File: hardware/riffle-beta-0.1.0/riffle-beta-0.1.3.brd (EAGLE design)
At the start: 104.8 x 18 mm, 46 parts, among them IC1 ATMEGA328P, IC3 CH340G, IC4 MCP1700-33, IC5 24AA128SN, IC6 MCP1700-33, J1 AYZ0202, U1 MCP73831T-2ACI/OT, X2 12MHz, X3 16 MHz

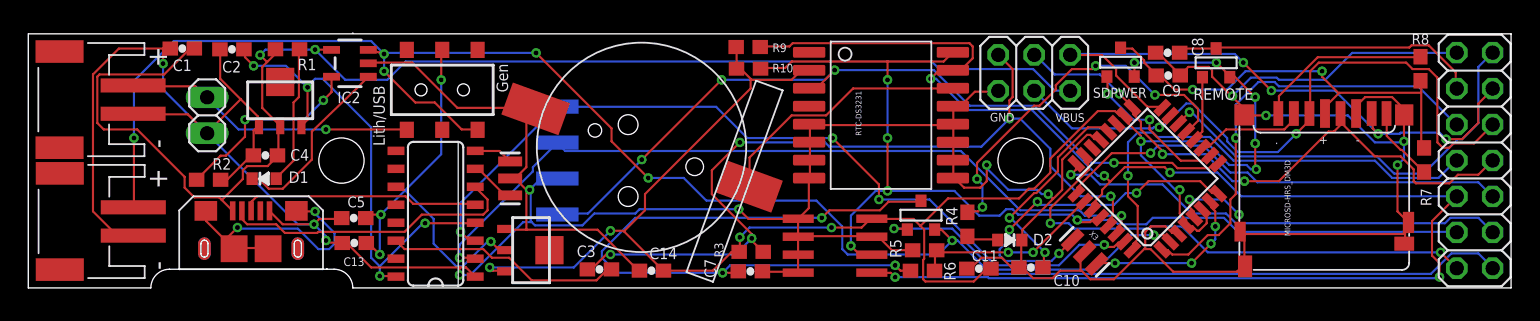
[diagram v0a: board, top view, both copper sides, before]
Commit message: tightened USB cutout; moved via away from left screw
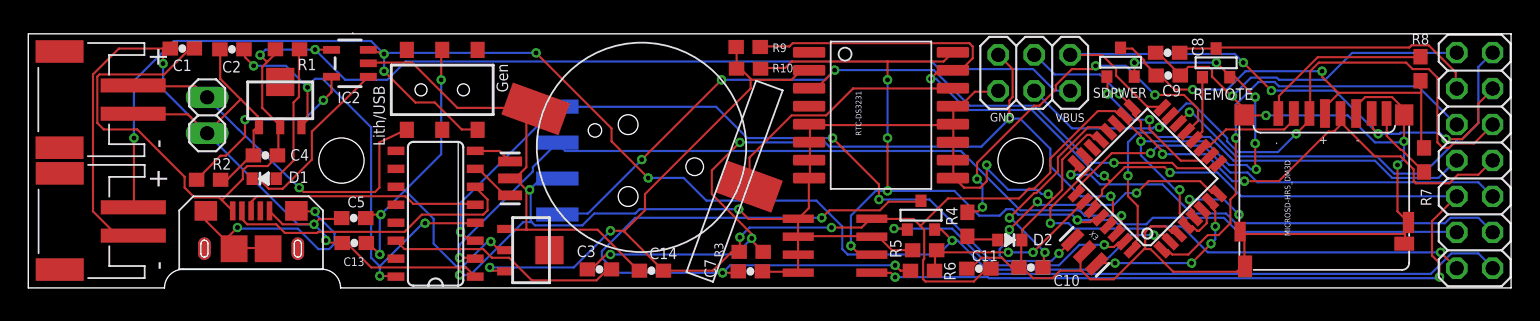
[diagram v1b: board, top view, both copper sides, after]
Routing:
- net VGEN: track 20.7 -> 26.0 mm
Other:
- outline, holes or cut-outs redrawn
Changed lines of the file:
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@@
 <text x="1.5494" y="2.54" size="1.016" layer="22" rot="MR90">3.7V</text>
 <wire x1="-2.1336" y1="17.9578" x2="102.6668" y2="17.9578" width="0" layer="20"/>
-<wire x1="20.8026" y1="0" x2="102.6668" y2="0" width="0" layer="20"/>
+<wire x1="19.939" y1="0" x2="102.6668" y2="0" width="0" layer="20"/>
 <wire x1="102.6668" y1="17.9578" x2="102.6668" y2="0" width="0" layer="20"/>
-<wire x1="-2.1336" y1="0" x2="6.5278" y2="0" width="0" layer="20"/>
-<wire x1="6.5278" y1="0" x2="7.8486" y2="1.3208" width="0" layer="20" curve="-90"/>
-<wire x1="7.8486" y1="1.3208" x2="18.9738" y2="1.3208" width="0" layer="20"/>
-<wire x1="18.9738" y1="1.3208" x2="18.9738" y2="1.3462" width="0" layer="20"/>
-<wire x1="18.9738" y1="1.3208" x2="19.4818" y2="1.3208" width="0" layer="20"/>
-<wire x1="19.4818" y1="1.3208" x2="20.8026" y2="0" width="0" layer="20" curve="-90"/>
+<wire x1="-2.1336" y1="0" x2="7.493" y2="0" width="0" layer="20"/>
+<wire x1="7.493" y1="0" x2="8.8138" y2="1.3208" width="0" layer="20" curve="-90"/>
+<wire x1="8.8138" y1="1.3208" x2="18.6182" y2="1.3208" width="0" layer="20"/>
+<wire x1="18.6182" y1="1.3208" x2="19.939" y2="0" width="0" layer="20" curve="-90"/>
 <text x="65.8368" y="11.7602" size="0.6096" layer="21">GND</text>
 <text x="70.4596" y="11.7348" size="0.6096" layer="21">VBUS</text>
@@
 <contactref element="J1" pad="4"/>
 <contactref element="JP1" pad="2"/>
-<wire x1="18.8976" y1="11.2014" x2="24.6126" y2="11.2014" width="0.1524" layer="1"/>
-<wire x1="12.7254" y1="11.2014" x2="18.8976" y2="11.2014" width="0.1524" layer="16"/>
+<wire x1="17.018" y1="7.0866" x2="17.3228" y2="6.7818" width="0.1524" layer="1"/>
+<wire x1="17.3228" y1="6.7818" x2="22.3774" y2="6.7818" width="0.1524" layer="1"/>
+<wire x1="22.3774" y1="6.7818" x2="22.6822" y2="7.0866" width="0.1524" layer="1"/>
+<wire x1="22.6822" y1="7.0866" x2="22.6822" y2="10.287" width="0.1524" layer="1"/>
+<wire x1="22.6822" y1="10.287" x2="24.6126" y2="11.2014" width="0.1524" layer="1"/>
+<wire x1="12.7254" y1="11.2014" x2="17.018" y2="7.0866" width="0.1524" layer="16"/>
 <wire x1="10.5156" y1="13.4112" x2="12.7254" y2="11.2014" width="0.1524" layer="16"/>
 <wire x1="24.6126" y1="11.2014" x2="24.6226" y2="11.1742" width="0.1524" layer="1"/>
@@
 <wire x1="5.334" y1="14.2494" x2="5.2748" y2="14.3096" width="0.1524" layer="1"/>
 <wire x1="10.4394" y1="13.4874" x2="10.509" y2="13.4696" width="0.1524" layer="1"/>
-<via x="18.8976" y="11.2014" extent="1-16" drill="0.3302"/>
+<via x="17.018" y="7.0866" extent="1-16" drill="0.3302"/>
 </signal>
 <signal name="N$6">
